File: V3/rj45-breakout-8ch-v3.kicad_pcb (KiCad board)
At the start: 2 copper layers, 93 x 67.8 mm, 14 parts, among them J1 Jack RJ45, J10 SWITCHES1, J11 SWITCHES2, J12 SWITCHES3, J13 SWITCHES4, J2 Jack RJ45, J3 Jack RJ45, J4 Jack RJ45, J5 Jack RJ45, J6 Jack RJ45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

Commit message: Bla
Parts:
- moved Ref** 33.0 mm to (175.0, 112.0)

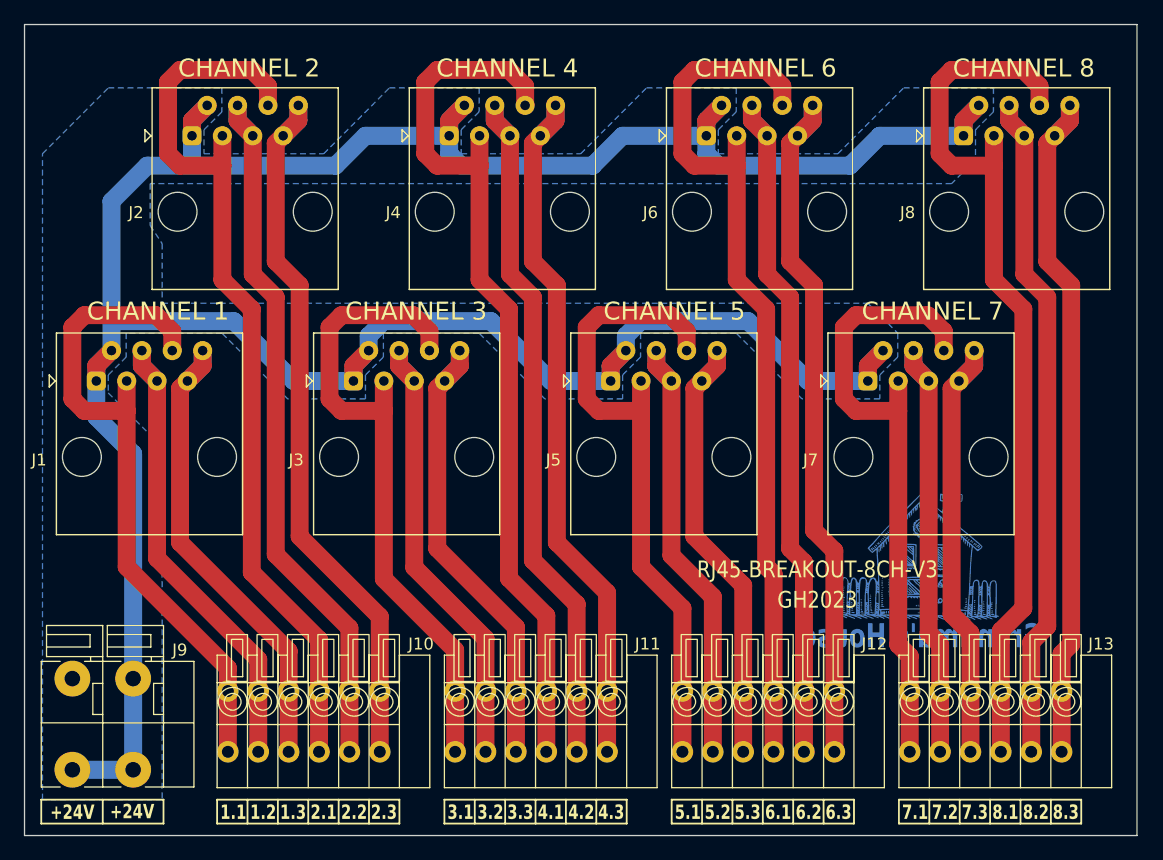
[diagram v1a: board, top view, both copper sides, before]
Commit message: Cosmetic enhancements to PCB
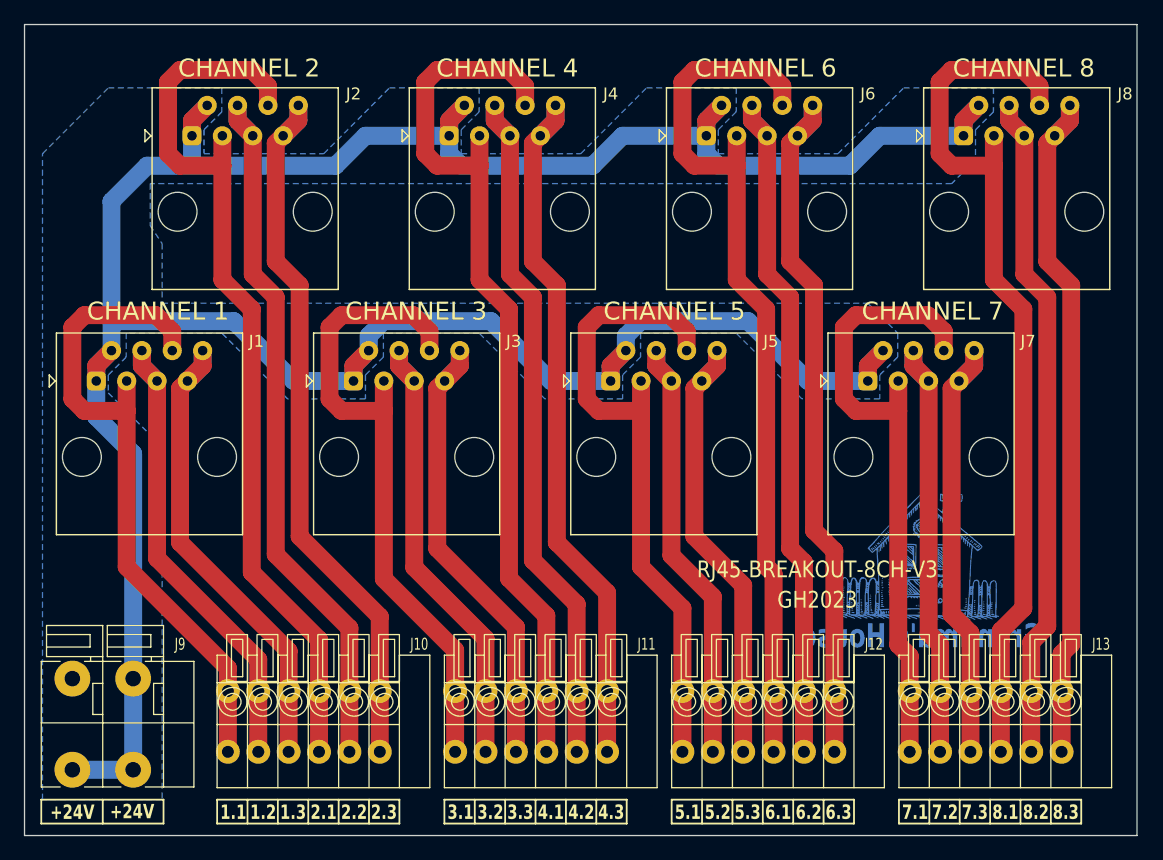
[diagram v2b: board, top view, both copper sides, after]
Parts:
- J10: value SWITCHES1 -> DB141V-2.54-6P; footprint Tales:TerminalBlock_DB141V-2.54-6P_1x06_P2.54mm_Vertical -> Tales:TerminalBlock_Dibo_DB141V-2.54-6P_1x06_P2.54mm_Vertical
- J11: value SWITCHES2 -> DB141V-2.54-6P; footprint Tales:TerminalBlock_DB141V-2.54-6P_1x06_P2.54mm_Vertical -> Tales:TerminalBlock_Dibo_DB141V-2.54-6P_1x06_P2.54mm_Vertical
- J12: value SWITCHES3 -> DB141V-2.54-6P; footprint Tales:TerminalBlock_DB141V-2.54-6P_1x06_P2.54mm_Vertical -> Tales:TerminalBlock_Dibo_DB141V-2.54-6P_1x06_P2.54mm_Vertical
- J13: value SWITCHES4 -> DB141V-2.54-6P; footprint Tales:TerminalBlock_DB141V-2.54-6P_1x06_P2.54mm_Vertical -> Tales:TerminalBlock_Dibo_DB141V-2.54-6P_1x06_P2.54mm_Vertical
- J9: value 24V -> DB142V-5.08-2P; footprint Tales:TerminalBlock_DB142V-2-5.08_1x02_P5.08mm_Vertical -> Tales:TerminalBlock_Dibo_DB142V-2-5.08_1x02_P5.08mm_Vertical

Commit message: New image
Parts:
- removed Ref**: Val**, Tales:Grandmas_medium_bottom
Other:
- board text added: "2023 TMASCHIO"
- board text removed: "GH2023"
- board text removed: "Grandma's House"
